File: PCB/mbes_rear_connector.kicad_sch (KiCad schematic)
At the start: 1 part

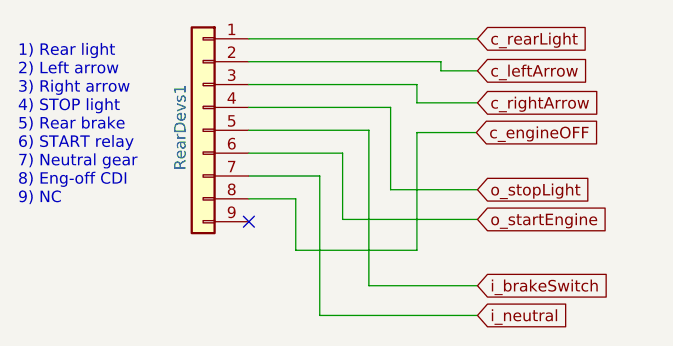
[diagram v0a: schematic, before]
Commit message: Fixes and optimizations (unuseful I/O lines dropped)
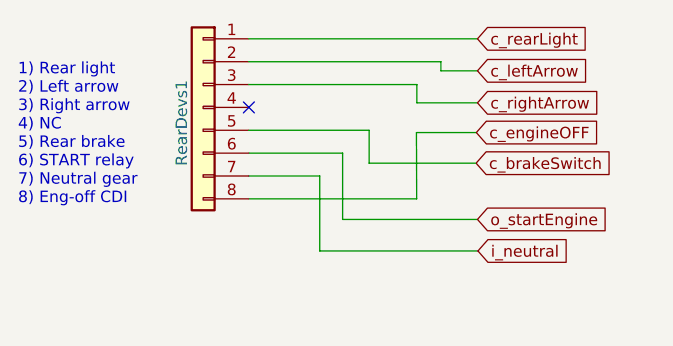
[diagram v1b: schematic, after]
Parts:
- removed RearDevs1: Conn_01x09, Connector_PinHeader_2.54mm:PinHeader_1x09_P2.54mm_Vertical, symbol Connector_Generic:Conn_01x09
- added RearDevs1: Conn_01x08, Connector_PinHeader_2.54mm:PinHeader_1x08_P2.54mm_Vertical, symbol Connector_Generic:Conn_01x08
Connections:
- net c_engineOFF: now also RearDevs1.8 (Pin_8)
- net c_leftArrow: now also RearDevs1.2 (Pin_2)
- net c_rearLight: now also RearDevs1.1 (Pin_1)
- net c_rightArrow: now also RearDevs1.3 (Pin_3)
- net i_neutral: now also RearDevs1.7 (Pin_7)
- net o_startEngine: now also RearDevs1.6 (Pin_6)
- new net c_brakeSwitch: RearDevs1.5 (Pin_5)
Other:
- note added: "1) Rear light 2) Left arrow 3) Right arrow 4) NC 5) Rear brake 6) START relay 7) Neutral gear 8) Eng-off CDI"
- note removed: "1) Rear light 2) Left arrow 3) Right arrow 4) STOP light 5) Rear brake 6) START relay 7) Neutral gear 8) Eng-off CDI 9) NC"
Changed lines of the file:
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@@
 (kicad_sch (version 20211123) (generator eeschema)
   (paper "A4")
-  (no_connect (at 72.644 70.358))
-  (wire (pts (xy 80.518 80.772) (xy 98.044 80.772))
-    (stroke (width 0) (type default) (color 0 0 0 0))
-  )
+  (no_connect (at 72.644 57.658))
   (wire (pts (xy 72.644 52.578) (xy 93.98 52.578))
     (stroke (width 0) (type default) (color 0 0 0 0))
@@
     (stroke (width 0) (type default) (color 0 0 0 0))
   )
-  (wire (pts (xy 77.851 73.533) (xy 91.313 73.533))
-    (stroke (width 0) (type default) (color 0 0 0 0))
-  )
-  (wire (pts (xy 72.644 57.658) (xy 88.392 57.658))
-    (stroke (width 0) (type default) (color 0 0 0 0))
-  )
   (wire (pts (xy 72.644 65.278) (xy 80.518 65.278))
     (stroke (width 0) (type default) (color 0 0 0 0))
   )
-  (wire (pts (xy 77.851 67.818) (xy 77.851 73.533))
-    (stroke (width 0) (type default) (color 0 0 0 0))
-  )
-  (wire (pts (xy 85.979 60.198) (xy 85.979 77.47))
+  (wire (pts (xy 86.0044 63.8556) (xy 86.0044 60.198))
     (stroke (width 0) (type default) (color 0 0 0 0))
   )
@@
     (stroke (width 0) (type default) (color 0 0 0 0))
   )
-  (wire (pts (xy 72.644 60.198) (xy 85.979 60.198))
+  (wire (pts (xy 72.644 60.198) (xy 86.0044 60.198))
     (stroke (width 0) (type default) (color 0 0 0 0))
   )
@@
     (stroke (width 0) (type default) (color 0 0 0 0))
   )
+  (wire (pts (xy 80.518 73.6092) (xy 98.0948 73.6092))
+    (stroke (width 0) (type default) (color 0 0 0 0))
+  )
   (wire (pts (xy 93.98 53.594) (xy 98.044 53.594))
     (stroke (width 0) (type default) (color 0 0 0 0))
   )
-  (wire (pts (xy 91.313 73.533) (xy 91.313 60.452))
-    (stroke (width 0) (type default) (color 0 0 0 0))
-  )
-  (wire (pts (xy 85.979 77.47) (xy 98.044 77.47))
-    (stroke (width 0) (type default) (color 0 0 0 0))
-  )
-  (wire (pts (xy 88.392 66.802) (xy 98.044 66.802))
+  (wire (pts (xy 91.2876 67.818) (xy 91.2622 60.452))
     (stroke (width 0) (type default) (color 0 0 0 0))
   )
@@
     (stroke (width 0) (type default) (color 0 0 0 0))
   )
-  (wire (pts (xy 88.392 57.658) (xy 88.392 66.802))
-    (stroke (width 0) (type default) (color 0 0 0 0))
-  )
   (wire (pts (xy 72.644 50.038) (xy 98.044 50.038))
     (stroke (width 0) (type default) (color 0 0 0 0))
   )
-  (wire (pts (xy 91.313 60.452) (xy 97.917 60.452))
+  (wire (pts (xy 97.8916 63.8556) (xy 86.0044 63.8556))
     (stroke (width 0) (type default) (color 0 0 0 0))
   )
-  (wire (pts (xy 80.518 65.278) (xy 80.518 80.772))
+  (wire (pts (xy 91.2622 60.452) (xy 97.917 60.452))
+    (stroke (width 0) (type default) (color 0 0 0 0))
+  )
+  (wire (pts (xy 80.518 65.278) (xy 80.518 73.6092))
     (stroke (width 0) (type default) (color 0 0 0 0))
   )
@@
     (stroke (width 0) (type default) (color 0 0 0 0))
   )
-  (wire (pts (xy 72.644 67.818) (xy 77.851 67.818))
+  (wire (pts (xy 72.644 67.818) (xy 91.2876 67.818))
     (stroke (width 0) (type default) (color 0 0 0 0))
   )
-  (text "1) Rear light\n2) Left arrow\n3) Right arrow\n4) STOP light\n5) Rear brake\n6) START relay\n7) Neutral gear\n8) Eng-off CDI\n9) NC"
+  (text "1) Rear light\n2) Left arrow\n3) Right arrow\n4) NC\n5) Rear brake\n6) START relay\n7) Neutral gear\n8) Eng-off CDI"
     (at 46.99 68.58 0)
     (effects (font (size 1.27 1.27)) (justify left bottom))
@@
     )
   )
-  (global_label "i_neutral" (shape input) (at 98.044 80.772 0) (fields_autoplaced)
+  (global_label "i_neutral" (shape input) (at 98.0948 73.6092 0) (fields_autoplaced)
     (effects (font (size 1.27 1.27)) (justify left))
-    (property "Riferimenti inter-foglio" "${INTERSHEET_REFS}" (id 0) (at 108.7423 80.6926 0)
+    (property "Riferimenti inter-foglio" "${INTERSHEET_REFS}" (id 0) (at 108.7931 73.5298 0)
       (effects (font (size 1.27 1.27)) (justify left) hide)
     )
@@
     )
   )
-  (global_label "i_brakeSwitch" (shape input) (at 98.044 77.47 0) (fields_autoplaced)
+  (global_label "c_brakeSwitch" (shape input) (at 97.8916 63.8556 0) (fields_autoplaced)
     (effects (font (size 1.27 1.27)) (justify left))
-    (property "Riferimenti inter-foglio" "${INTERSHEET_REFS}" (id 0) (at 113.3385 77.3906 0)
+    (property "Riferimenti inter-foglio" "${INTERSHEET_REFS}" (id 0) (at 113.6699 63.7762 0)
       (effects (font (size 1.27 1.27)) (justify left) hide)
     )
@@
     )
   )
-  (global_label "o_stopLight" (shape input) (at 98.044 66.802 0) (fields_autoplaced)
-    (effects (font (size 1.27 1.27)) (justify left))
-    (property "Riferimenti inter-foglio" "${INTERSHEET_REFS}" (id 0) (at 111.2823 66.7226 0)
-      (effects (font (size 1.27 1.27)) (justify left) hide)
-    )
-  )
   (global_label "c_engineOFF" (shape input) (at 97.917 60.452 0) (fields_autoplaced)
     (effects (font (size 1.27 1.27)) (justify left))
@@
     )
   )
-  (symbol (lib_id "Connector_Generic:Conn_01x09") (at 67.564 60.198 0) (mirror y) (unit 1)
+  (symbol (lib_id "Connector_Generic:Conn_01x08") (at 67.564 57.658 0) (mirror y) (unit 1)
     (in_bom yes) (on_board yes)
-    (property "Reference" "RearDevs1" (id 0) (at 65.024 64.643 90)
-      (effects (font (size 1.27 1.27)) (justify left))
-    )
-    (property "Value" "Conn_01x09" (id 1) (at 65.024 61.4679 0)
-      (effects (font (size 1.27 1.27)) (justify left) hide)
-    )
-    (property "Footprint" "Connector_PinHeader_2.54mm:PinHeader_1x09_P2.54mm_Vertical" (id 2) (at 67.564 60.198 0)
+    (property "Reference" "RearDevs1" (id 0) (at 65.1764 59.3852 90))
+    (property "Value" "Conn_01x08" (id 1) (at 67.564 71.9328 0)
       (effects (font (size 1.27 1.27)) hide)
     )
-    (property "Datasheet" "~" (id 3) (at 67.564 60.198 0)
+    (property "Footprint" "Connector_PinHeader_2.54mm:PinHeader_1x08_P2.54mm_Vertical" (id 2) (at 67.564 57.658 0)
+      (effects (font (size 1.27 1.27)) hide)
+    )
+    (property "Datasheet" "~" (id 3) (at 67.564 57.658 0)
       (effects (font (size 1.27 1.27)) hide)
     )
@@
     (pin "7")
     (pin "8")
-    (pin "9")
   )
 )

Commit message: PCB splitted
In order to use the debug support, it has been needed to add the ISP port. But it means to loose 4 pins.
So, I have added a I/O extender chip on I2C bus (other 2 pins lost). Because the complexity has encreased
I have had to split the PCB in thwo different ones.
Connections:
- net c_rearLight renamed i_lightON/OFF
- net o_startEngine renamed c_startEngine
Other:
- company: (none) -> Panicosoft
- title: (none) -> Motorbike lights and services controller
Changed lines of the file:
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@@
 (kicad_sch (version 20211123) (generator eeschema)
   (paper "A4")
+  (title_block
+    (title "Motorbike lights and services controller")
+    (rev "4.0")
+    (company "Panicosoft")
+    (comment 1 "Logic controller unit")
+    (comment 2 "Connector to the rear motorbike side services")
+  )
   (no_connect (at 72.644 57.658))
   (wire (pts (xy 72.644 52.578) (xy 93.98 52.578))
@@
     (effects (font (size 1.27 1.27)) (justify left bottom))
   )
-  (global_label "o_startEngine" (shape input) (at 98.044 70.104 0) (fields_autoplaced)
+  (global_label "c_startEngine" (shape input) (at 98.044 70.104 0) (fields_autoplaced)
     (effects (font (size 1.27 1.27)) (justify left))
-    (property "Riferimenti inter-foglio" "${INTERSHEET_REFS}" (id 0) (at 113.2781 70.0246 0)
+    (property "Riferimenti inter-foglio" "${INTERSHEET_REFS}" (id 0) (at 113.2176 70.0246 0)
       (effects (font (size 1.27 1.27)) (justify left) hide)
     )
@@
     )
   )
-  (global_label "c_rearLight" (shape input) (at 98.044 50.038 0) (fields_autoplaced)
-    (effects (font (size 1.27 1.27)) (justify left))
-    (property "Riferimenti inter-foglio" "${INTERSHEET_REFS}" (id 0) (at 110.98 49.9586 0)
-      (effects (font (size 1.27 1.27)) (justify left) hide)
-    )
-  )
   (global_label "c_brakeSwitch" (shape input) (at 97.8916 63.8556 0) (fields_autoplaced)
     (effects (font (size 1.27 1.27)) (justify left))
@@
       (effects (font (size 1.27 1.27)) (justify left) hide)
     )
+  )
+  (global_label "i_lightON{slash}OFF" (shape input) (at 98.044 50.038 0) (fields_autoplaced)
+    (effects (font (size 1.27 1.27)) (justify left))
+    (property "Riferimenti inter-foglio" "${INTERSHEET_REFS}" (id 0) (at 113.8223 49.9586 0)
+      (effects (font (size 1.27 1.27)) (justify left) hide)
+    )
